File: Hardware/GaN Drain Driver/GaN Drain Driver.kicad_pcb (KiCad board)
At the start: 2 copper layers, 50.8 x 50.8 mm, 14 parts, among them J1 Conn_Coaxial, Q1 IRFS4321, U1 IRS2005S

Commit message: Updating drain driver board
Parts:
- added H1: 4-40, _tim-Mounting-Holes:4-40_Hole_Pad, F.Cu at (136.5, 28.6)
- added H2: 4-40, _tim-Mounting-Holes:4-40_Hole_Pad, F.Cu at (54.0, 28.6)
- added H3: 4-40, _tim-Mounting-Holes:4-40_Hole_Pad, F.Cu at (136.5, 60.3)
- added H4: 4-40, _tim-Mounting-Holes:4-40_Hole_Pad, F.Cu at (54.0, 60.3)
- moved R2 125.6 mm to (59.1, 41.3), turned to 180 degrees
- moved U1 122.5 mm to (63.5, 50.8)
- moved R1 120.4 mm to (63.5, 55.2)
- moved D1 113.1 mm to (63.5, 46.4), turned to 180 degrees
- moved C1 111.4 mm to (69.8, 49.9), turned to -90 degrees
- moved C2 93.3 mm to (82.1, 36.6), turned to 90 degrees
- moved Q1 69.5 mm to (127.7, 44.5)
- moved C6 67.2 mm to (96.5, 49.6), turned to -90 degrees
- moved C7 53.2 mm to (109.9, 49.8), turned to -90 degrees
- moved C9 26.3 mm to (67.9, 31.8), turned to -90 degrees
- moved C3 19.0 mm to (95.9, 36.6), turned to 90 degrees
- moved C4 19.0 mm to (110.0, 36.6), turned to 90 degrees
- moved C5 9.14 mm to (82.5, 54.4), turned to 90 degrees
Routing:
- added copper zone on F.Cu, net VCC
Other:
- board size 50.8 x 50.8 mm -> 88.9 x 38.1 mm

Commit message: Updating drain driver board
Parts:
- added C8: 100nF, Capacitor_SMD:C_0805_2012Metric, F.Cu at (70.2, 27.9)
- added J2: Conn_01x02_Socket, Connector_PinSocket_2.54mm:PinSocket_1x02_P2.54mm_Vertical, F.Cu at (136.7, 37.3)
- added J3: Conn_01x02_Socket, Connector_PinSocket_2.54mm:PinSocket_1x02_P2.54mm_Vertical, F.Cu at (73.9, 27.9)
- added J4: Conn_01x02_Socket, Connector_PinSocket_2.54mm:PinSocket_1x02_P2.54mm_Vertical, F.Cu at (125.1, 28.6)
- moved C9 20.0 mm to (66.0, 51.7)
- moved J1 13.7 mm to (63.5, 27.5), turned to 180 degrees
- moved C1 11.1 mm to (72.4, 39.1)
- moved D1 11.1 mm to (66.0, 35.6)
- moved R1 11.1 mm to (66.0, 44.5)
- moved U1 11.1 mm to (66.0, 40.0)
- moved C5 5.81 mm to (84.5, 48.9), turned to -90 degrees
- moved Q1 5.23 mm to (128.9, 49.5)
- moved C4 4.55 mm to (113.0, 40.0)
- moved C3 4.24 mm to (98.4, 40.0)
- moved C2 4.16 mm to (84.5, 40.0)
- moved C7 3.29 mm to (113.0, 48.9)
- moved R2 2.25 mm to (59.7, 39.1), turned to -90 degrees
- moved C6 2.03 mm to (98.4, 48.9)
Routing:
- net AMP_DRAIN: track 0.00 -> 88.2 mm, vias 0 -> 1
- net Net-(Q1-G): track 0.00 -> 80.4 mm
- net +15V: track 0.00 -> 33.8 mm, vias 0 -> 1
- net VCC: track 0.00 -> 21.9 mm
- net Net-(J1-In): track 0.00 -> 16.8 mm
- net Net-(U1-HO): track 0.00 -> 7.05 mm
- net Net-(D1-K): track 0.00 -> 6.76 mm
- added copper zone on F.Cu, net AMP_DRAIN
- added copper zone on B.Cu, net GND
- added copper zone on F.Cu, net GND
- added copper zone on B.Cu, net VCC
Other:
- outline, holes or cut-outs redrawn
- board text added: "${TITLE} ${REVISION} ${COMMENT1}"
- board text added: "+15V"
- board text added: "AMP DRAIN"
- board text added: "GND"
- board text added: "TTL IN"
- board text added: "VCC"

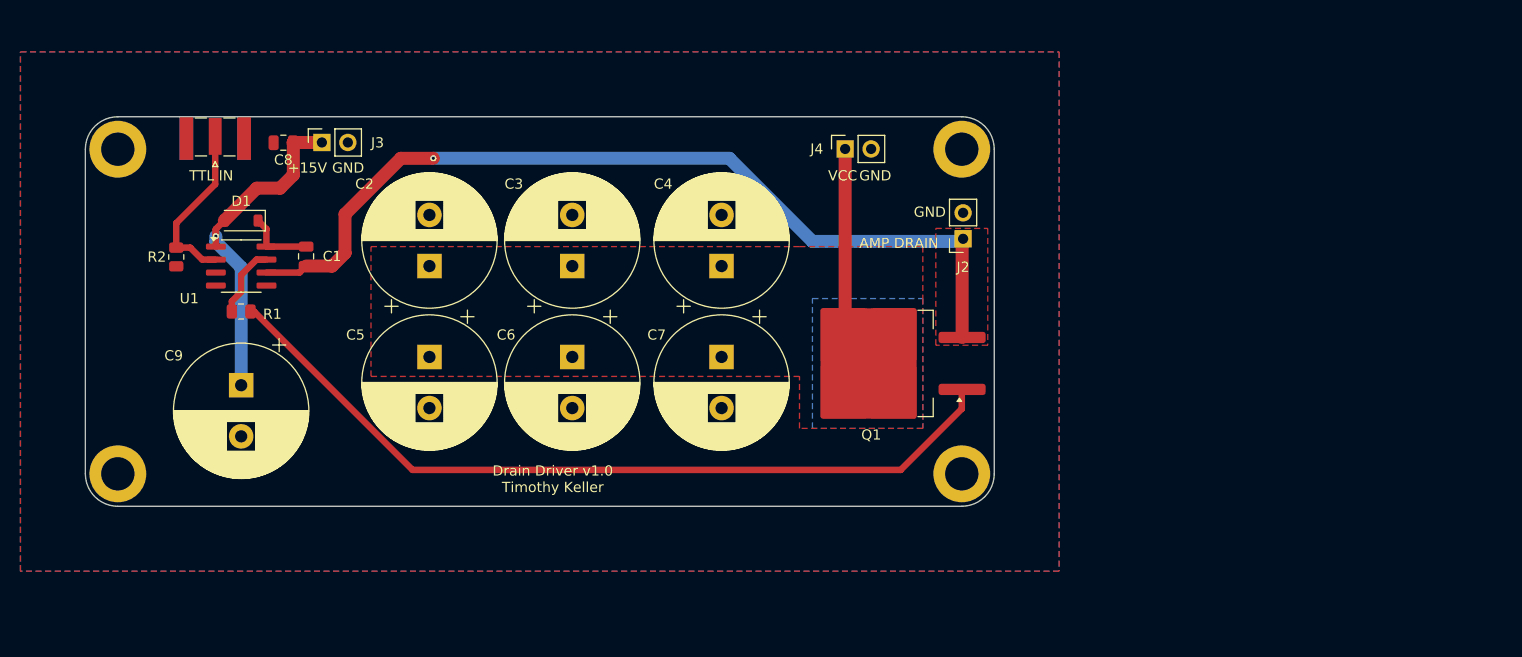
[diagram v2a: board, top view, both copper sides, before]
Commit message: Updated drain driver PCB
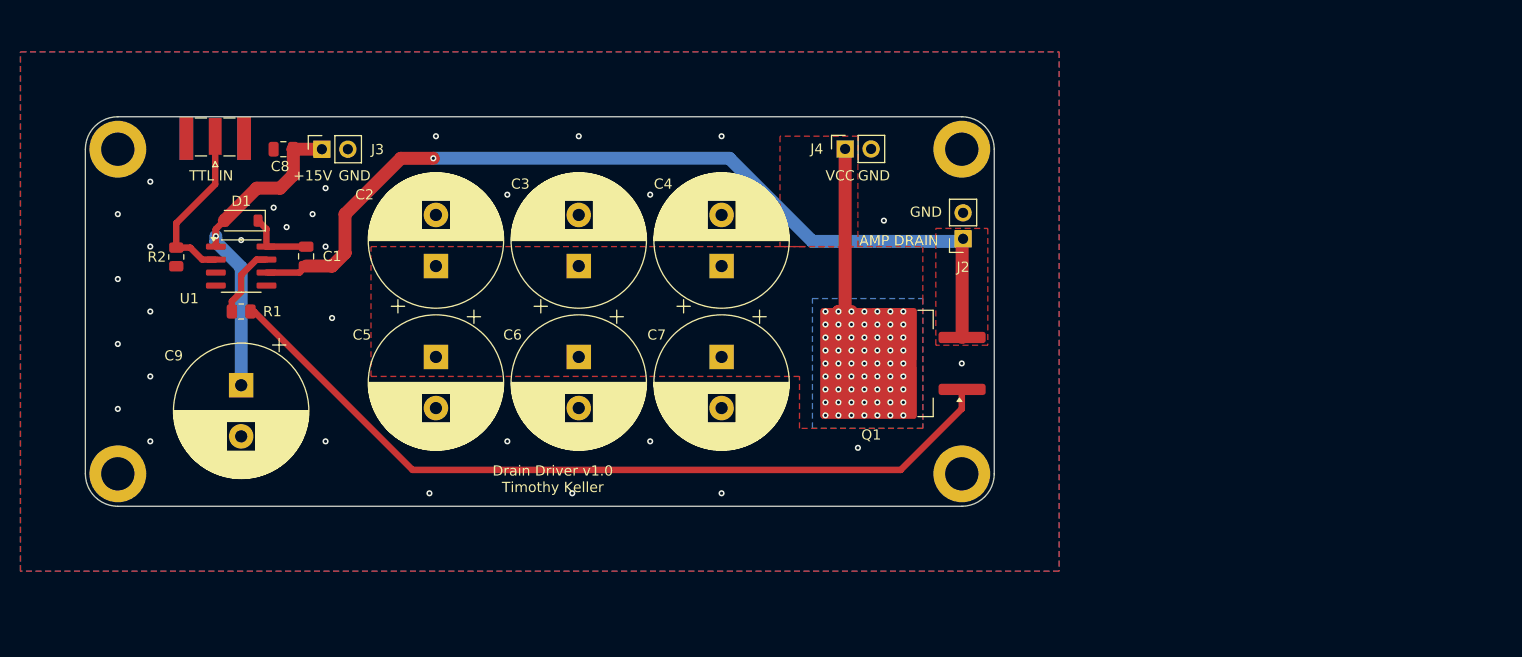
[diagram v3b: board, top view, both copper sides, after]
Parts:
- moved J3 0.66 mm to (73.9, 28.6)
- moved C6 0.64 mm to (99.1, 48.9)
- moved C2 0.64 mm to (85.1, 40.0)
- moved C3 0.64 mm to (99.1, 40.0)
- moved C5 0.64 mm to (85.1, 48.9)
- moved C8 0.63 mm to (70.2, 28.6)
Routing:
- net VCC: track 21.9 -> 28.0 mm, vias 0 -> 63
- net +15V: track 33.8 -> 33.1 mm
- net GND: vias 0 -> 30

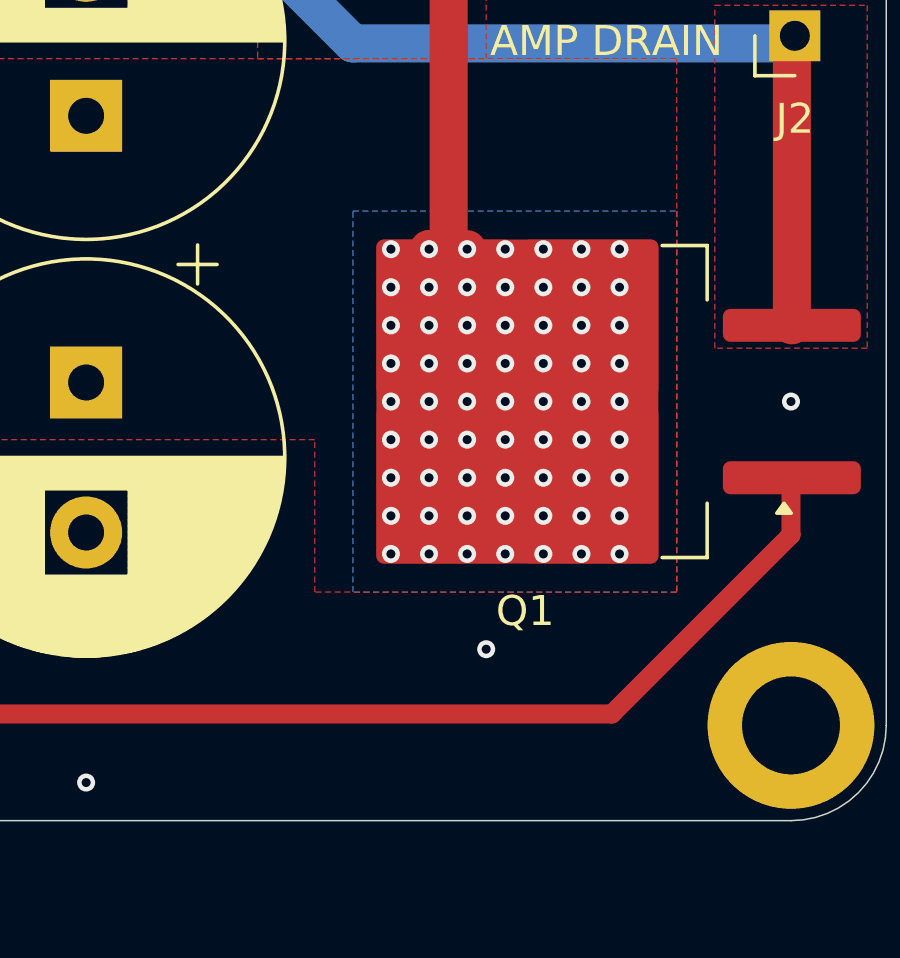
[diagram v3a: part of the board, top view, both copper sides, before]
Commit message: Added capacitors
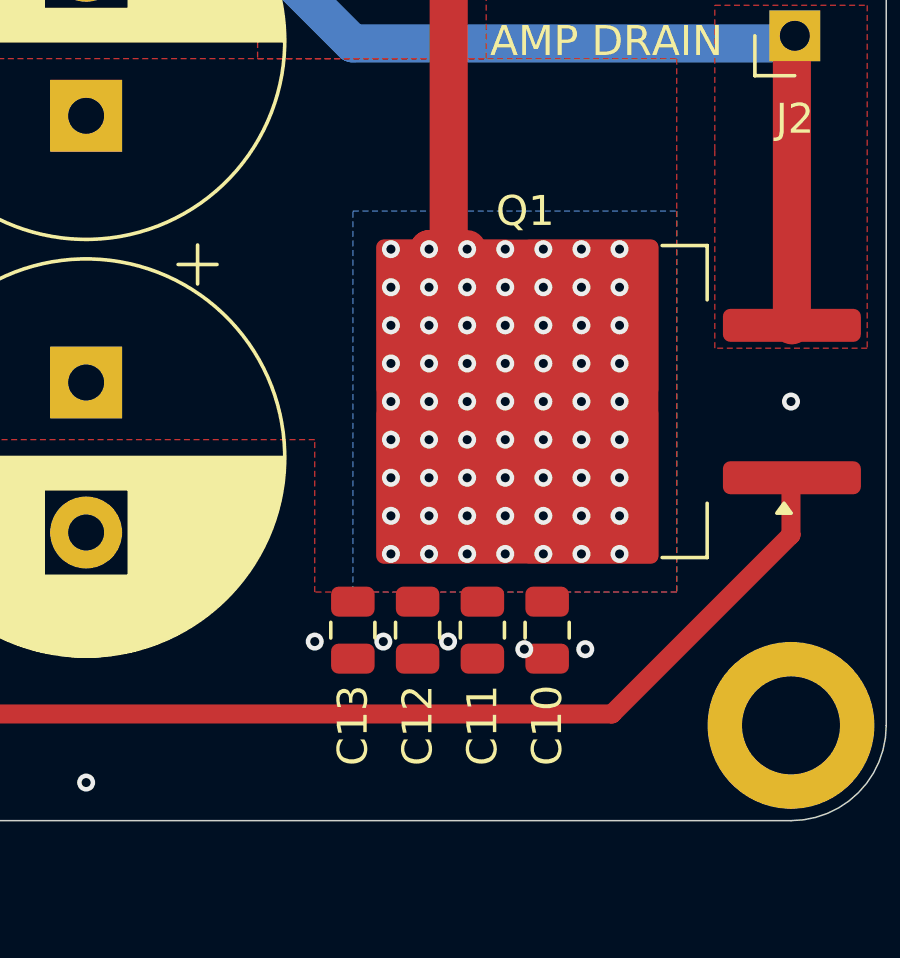
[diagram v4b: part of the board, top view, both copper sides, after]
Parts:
- added C10: 100nF, Capacitor_SMD:C_0805_2012Metric, F.Cu at (128.4, 57.1)
- added C11: 100nF, Capacitor_SMD:C_0805_2012Metric, F.Cu at (126.2, 57.1)
- added C12: 100nF, Capacitor_SMD:C_0805_2012Metric, F.Cu at (124.1, 57.1)
- added C13: 100nF, Capacitor_SMD:C_0805_2012Metric, F.Cu at (121.9, 57.1)
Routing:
- net GND: vias 30 -> 34

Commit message: Adding gerbers
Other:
- board text added: "INPUT"
- board text removed: "TTL IN"
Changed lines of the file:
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@@
 			(outputformat 1)
 			(mirror no)
-			(drillshape 1)
+			(drillshape 0)
 			(scaleselection 1)
-			(outputdirectory "")
+			(outputdirectory "gerbers")
 		)
 	)
@@
 			(size 1.025 1.4)
 			(layers "F.Cu" "F.Paste" "F.Mask")
-			(roundrect_rratio 0.243902)
+			(roundrect_rratio 0.243902439)
 			(net 8 "Net-(U1-HO)")
 			(pintype "passive")
@@
 			(size 1.025 1.4)
 			(layers "F.Cu" "F.Paste" "F.Mask")
-			(roundrect_rratio 0.243902)
+			(roundrect_rratio 0.243902439)
 			(net 7 "Net-(Q1-G)")
 			(pintype "passive")
@@
 			(size 4.6 1.1)
 			(layers "F.Cu" "F.Paste" "F.Mask")
-			(roundrect_rratio 0.227273)
+			(roundrect_rratio 0.2272727273)
 			(net 7 "Net-(Q1-G)")
 			(pinfunction "G")
@@
 			(size 4.55 5.25)
 			(layers "F.Cu" "F.Paste")
-			(roundrect_rratio 0.054945)
+			(roundrect_rratio 0.05494505495)
 			(net 3 "VCC")
 			(pinfunction "D")
@@
 			(size 4.55 5.25)
 			(layers "F.Cu" "F.Paste")
-			(roundrect_rratio 0.054945)
+			(roundrect_rratio 0.05494505495)
 			(net 3 "VCC")
 			(pinfunction "D")
@@
 			(size 9.4 10.8)
 			(layers "F.Cu" "F.Mask")
-			(roundrect_rratio 0.026596)
+			(roundrect_rratio 0.02659595745)
 			(net 3 "VCC")
 			(pinfunction "D")
@@
 			(size 4.55 5.25)
 			(layers "F.Cu" "F.Paste")
-			(roundrect_rratio 0.054945)
+			(roundrect_rratio 0.05494505495)
 			(net 3 "VCC")
 			(pinfunction "D")
@@
 			(size 4.55 5.25)
 			(layers "F.Cu" "F.Paste")
-			(roundrect_rratio 0.054945)
+			(roundrect_rratio 0.05494505495)
 			(net 3 "VCC")
 			(pinfunction "D")
@@
 			(size 4.6 1.1)
 			(layers "F.Cu" "F.Paste" "F.Mask")
-			(roundrect_rratio 0.227273)
+			(roundrect_rratio 0.2272727273)
 			(net 1 "AMP_DRAIN")
 			(pinfunction "S")
@@
 			(size 1.025 1.4)
 			(layers "F.Cu" "F.Paste" "F.Mask")
-			(roundrect_rratio 0.243902)
+			(roundrect_rratio 0.243902439)
 			(net 6 "Net-(J1-In)")
 			(pintype "passive")
@@
 			(size 1.025 1.4)
 			(layers "F.Cu" "F.Paste" "F.Mask")
-			(roundrect_rratio 0.243902)
+			(roundrect_rratio 0.243902439)
 			(net 4 "GND")
 			(pintype "passive")
@@
 			(font
 				(size 1 1)
-				(thickness 0.1)
+				(thickness 0.15)
 			)
 			(justify left bottom)
@@
 			(font
 				(size 1 1)
-				(thickness 0.1)
+				(thickness 0.15)
 			)
 			(justify left bottom)
 		)
 	)
-	(gr_text "TTL IN"
+	(gr_text "INPUT"
 		(at 60.96 31.75 0)
 		(layer "F.SilkS")
@@
 			(font
 				(size 1 1)
-				(thickness 0.1)
+				(thickness 0.15)
 			)
 			(justify left bottom)
@@
 			(font
 				(size 1 1)
-				(thickness 0.1)
+				(thickness 0.15)
 			)
 			(justify left bottom)
@@
 			(font
 				(size 1 1)
-				(thickness 0.1)
+				(thickness 0.15)
 			)
 			(justify left bottom)
@@
 			(font
 				(size 1 1)
-				(thickness 0.1)
+				(thickness 0.15)
 			)
 			(justify left bottom)
@@
 			(font
 				(size 1 1)
-				(thickness 0.1)
+				(thickness 0.15)
 			)
 			(justify bottom)
@@
 			(font
 				(size 1 1)
-				(thickness 0.1)
+				(thickness 0.15)
 			)
 			(justify left bottom)

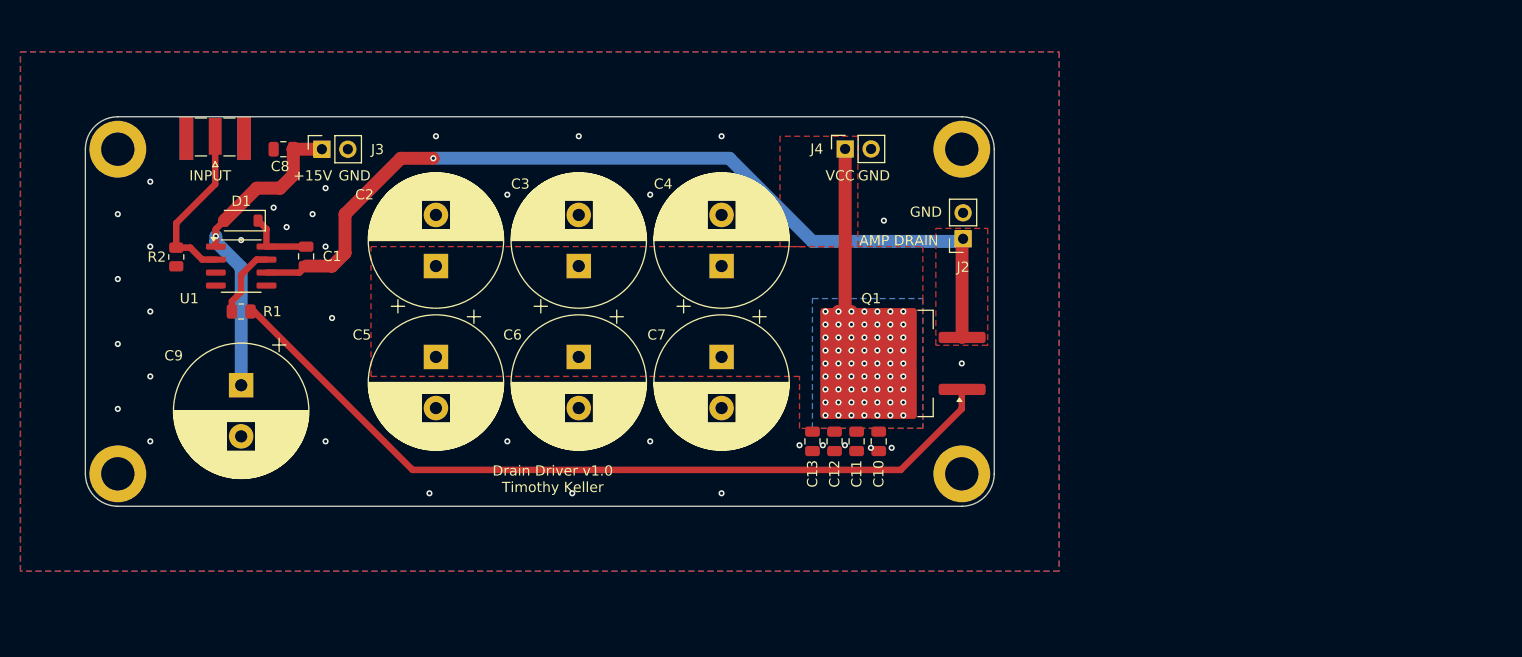
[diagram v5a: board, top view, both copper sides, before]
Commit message: Updating Drain Driver PCB
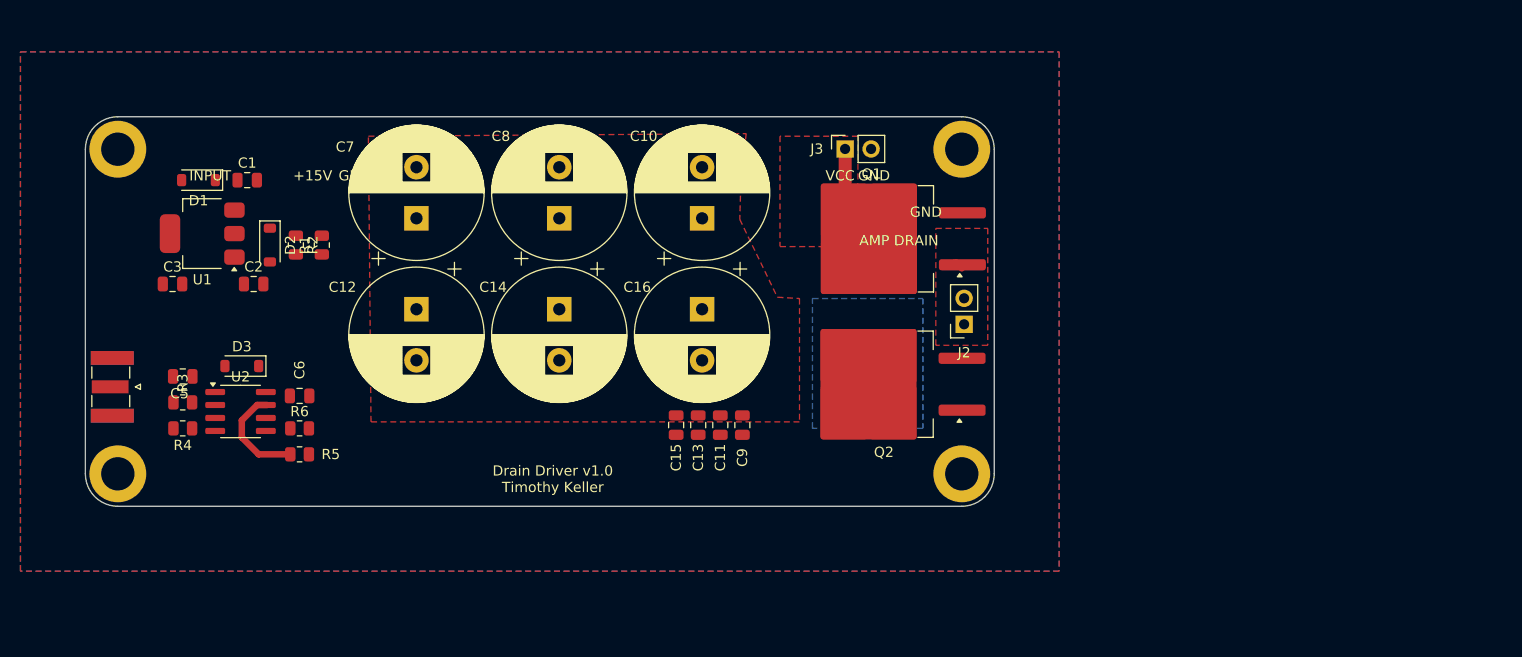
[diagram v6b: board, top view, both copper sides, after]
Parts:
- removed the C9 at (66.0, 51.7)
- removed the J3 at (73.9, 28.6)
- added C1: 100nF, Capacitor_SMD:C_0805_2012Metric, F.Cu at (66.6, 31.6)
- added C2: 100nF, Capacitor_SMD:C_0805_2012Metric, F.Cu at (67.3, 41.8)
- added C3: 1uF, Capacitor_SMD:C_0805_2012Metric, F.Cu at (59.3, 41.8)
- added D1: 1N5819HW-7-F, Diode_SMD:D_SOD-123, F.Cu at (61.9, 31.6)
- added D2: 1N5819HW-7-F, Diode_SMD:D_SOD-123, F.Cu at (68.8, 38.0)
- added Q2: IRFS4321, Package_TO_SOT_SMD:TO-263-2, F.Cu at (128.9, 51.6)
- added R1: 2.4k, Resistor_SMD:R_0805_2012Metric, F.Cu at (73.9, 38.0)
- added R2: 220, Resistor_SMD:R_0805_2012Metric, F.Cu at (71.4, 38.0)
- added R4: 10k, Resistor_SMD:R_0805_2012Metric, F.Cu at (60.3, 55.9)
- added R6: 33, Resistor_SMD:R_0805_2012Metric, F.Cu at (71.8, 55.9)
- added U2: IRS2008S, Package_SO:SOIC-8_3.9x4.9mm_P1.27mm, F.Cu at (66.0, 54.2)
- J1: value Conn_Coaxial -> SMA-J-P-H-ST-EM1
- U1: value IRS2005S -> LM317_SOT-223; footprint Package_SO:SOIC-8_3.9x4.9mm_P1.27mm -> Package_TO_SOT_SMD:SOT-223-3_TabPin2
- moved J1 26.3 mm to (53.4, 51.8), turned to -90 degrees
- moved C5 24.3 mm to (60.3, 50.8)
- moved R5 15.1 mm to (71.8, 58.4)
- moved R3 14.2 mm to (60.3, 53.3), turned to 180 degrees
- moved D3 14.2 mm to (66.1, 49.8)
- moved C6 13.7 mm to (71.8, 52.7), turned to 0 degrees
- moved C15 13.4 mm to (108.6, 55.6)
- moved C11 13.4 mm to (112.9, 55.6)
- moved C13 13.4 mm to (110.7, 55.6)
- moved C9 13.4 mm to (115.1, 55.6)
- moved Q1 12.2 mm to (128.9, 37.3)
- moved J2 8.36 mm to (136.8, 45.7)
- moved C10 5.04 mm to (111.1, 35.3)
- moved C12 5.04 mm to (83.2, 44.2)
- moved C14 5.04 mm to (97.2, 44.2)
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- renumbered C4 to C10, C5 to C12, C12 to C13, C6 to C14, C13 to C15, C7 to C16, C8 to C5, C1 to C6, C2 to C7, C3 to C8, C10 to C9, D1 to D3, J4 to J3, R2 to R3, R1 to R5
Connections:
- C6 pad 1: Net-(D1-K) -> Net-(D3-K)
- D3 pad 1: Net-(D1-K) -> Net-(D3-K)
- R5 pad 1: Net-(U1-HO) -> Net-(U2-HO)
- U1 pad 1: +15V -> Net-(D2-A)
- U1 pad 2: Net-(J1-In) -> +15V
- U1 pad 3: GND -> VCC
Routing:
- net AMP_DRAIN: track 88.2 -> 0.00 mm, vias 1 -> 0
- net Net-(Q1-G): track 80.4 -> 0.86 mm
- net +15V: track 33.1 -> 0.00 mm, vias 1 -> 0
- net VCC: track 28.0 -> 6.08 mm, vias 63 -> 0
- net Net-(J1-In): track 16.8 -> 0.00 mm
- net Net-(U2-HO): track 0.00 -> 10.2 mm
- net Net-(U1-HO): track 7.05 -> 0.00 mm
- net Net-(D1-K): track 6.76 -> 0.00 mm
- net GND: vias 34 -> 0

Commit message: updating board
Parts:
- added C4: 10uF, Capacitor_SMD:C_0805_2012Metric, F.Cu at (60.3, 44.5)
- added TP1: TestPoint, TestPoint:TestPoint_Pad_D1.0mm, F.Cu at (56.5, 43.2)
- moved R1 4.86 mm to (71.1, 41.9), turned to -90 degrees
- moved C13 4.48 mm to (114.9, 57.1)
- moved C15 4.48 mm to (112.8, 57.1)
- moved C9 4.48 mm to (119.3, 57.1)
- moved C11 4.48 mm to (117.1, 57.1)
- moved C2 2.49 mm to (64.8, 41.9), turned to 180 degrees
- moved C3 1.01 mm to (60.3, 41.9)
- moved D1 0.91 mm to (61.0, 31.6)
- moved D2 0.56 mm to (68.6, 37.5)
- moved R2 0.27 mm to (71.1, 38.0)
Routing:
- added copper zone on B.Cu, net AMP_DRAIN
